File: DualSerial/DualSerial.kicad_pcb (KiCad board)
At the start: 2 copper layers, 99.9 x 99.9 mm, 22 parts, among them CN1 DB9 Male, CN2 DB9 Male, J1 COM_A_SELECT, J2 IRQ_A_SELECT, J3 COM_A_SELECT, J4 IRQ_B_SELECT, J5 Bus_ISA_8bit, U1 16550/16C550, U2 GAL16V8, U3 GD75232N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

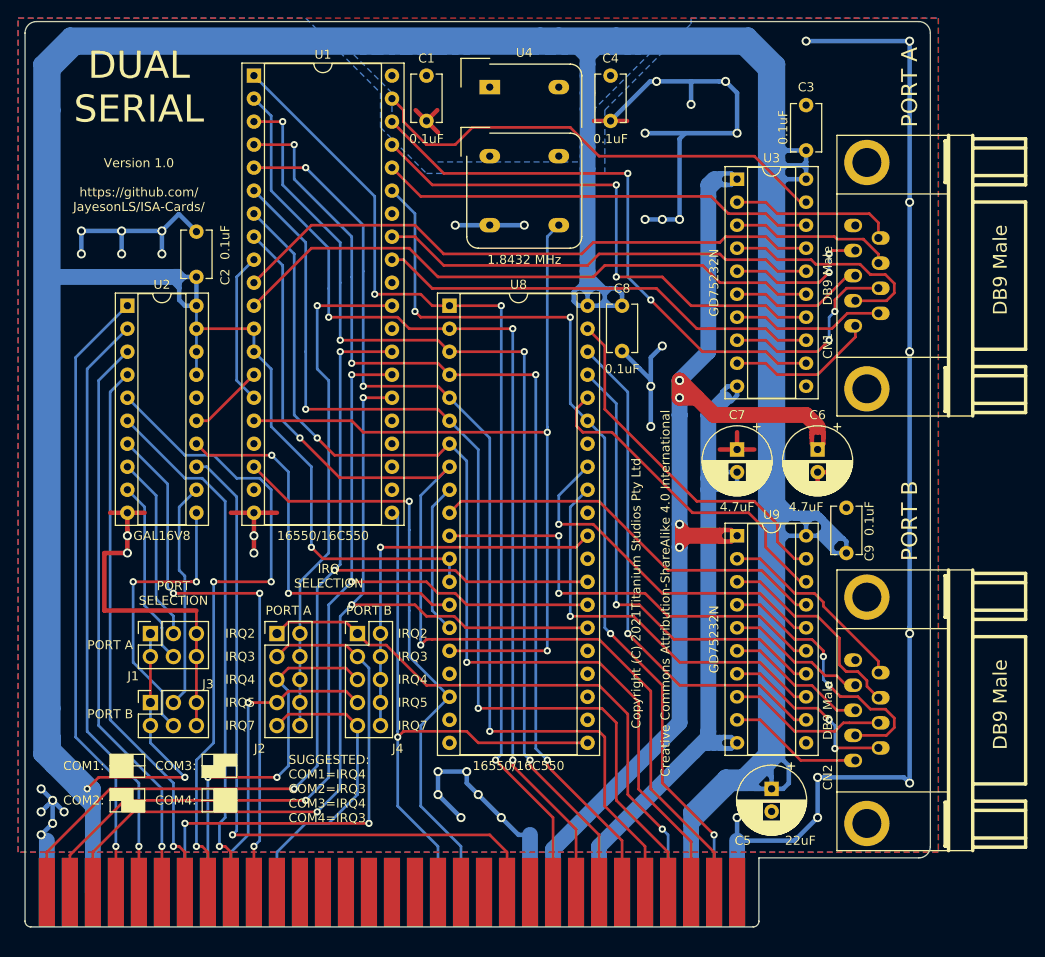
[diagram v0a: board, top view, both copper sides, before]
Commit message: DualSerial: Several PCB improvements, including adding a small piece of extra PCB to the bottom right for some additional strength around the DIN connector.
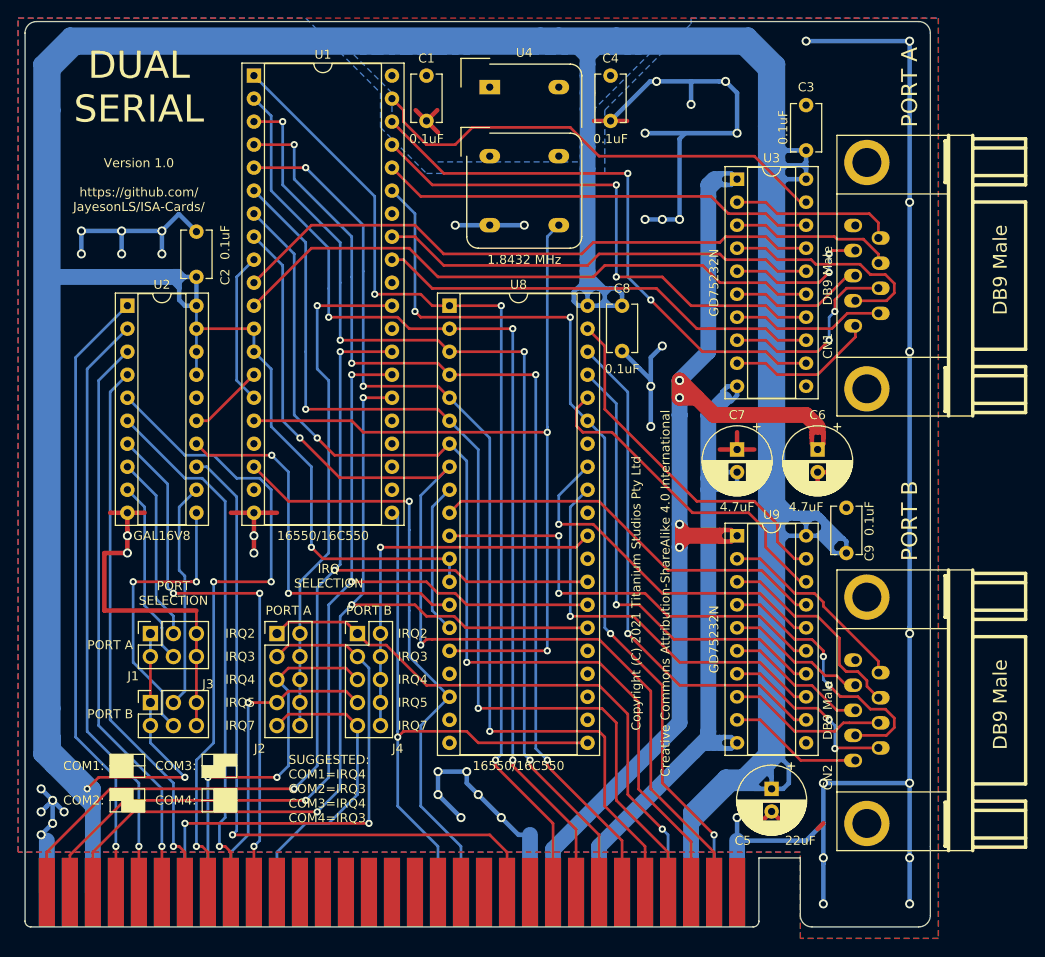
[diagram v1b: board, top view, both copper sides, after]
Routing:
- net GND: track 327.3 -> 355.3 mm, vias 44 -> 47
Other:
- outline, holes or cut-outs redrawn
- board text added: "Copyright (C) 2021 Titanium Studios Pty Ltd Creative Commons Attribution-ShareAlike 4.0 International"
- board text removed: "Copyright (C) 2021Titanium Studios Pty Ltd Creative Commons Attribution-ShareAlike 4.0 International"

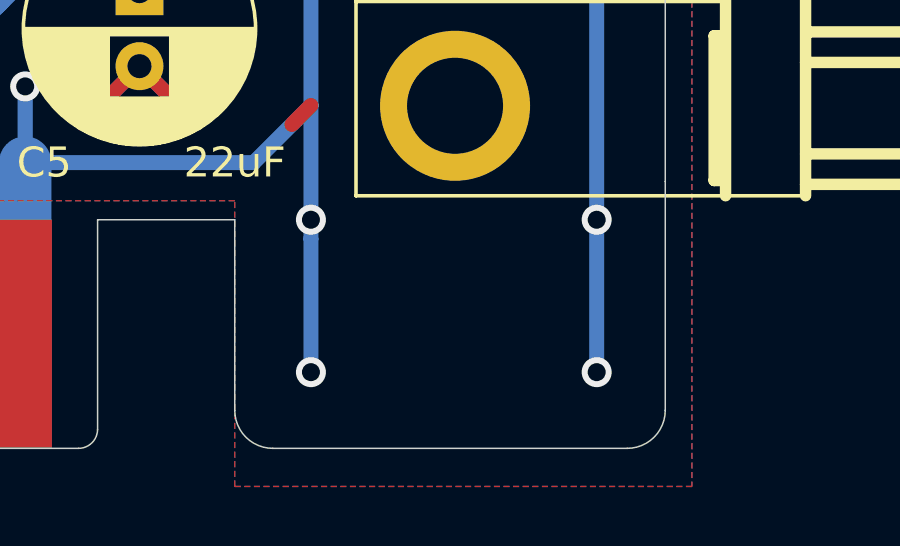
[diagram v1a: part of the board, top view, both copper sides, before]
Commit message: DualSerial: Reduce size of PCB tab added in the previous commit.
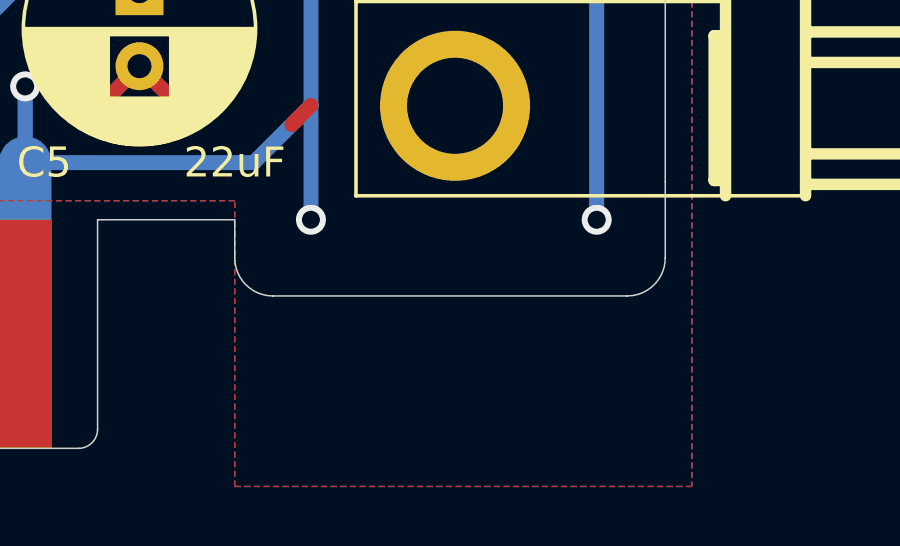
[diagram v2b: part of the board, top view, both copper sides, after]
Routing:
- net GND: track 355.3 -> 345.2 mm, vias 47 -> 45
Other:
- outline, holes or cut-outs redrawn

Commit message: Update boards.
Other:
- board text added: "Created by Jayeson Lee-Steere"
- board text removed: "Copyright (C) 2021 Titanium Studios Pty Ltd Creative Commons Attribution-ShareAlike 4.0 International"
